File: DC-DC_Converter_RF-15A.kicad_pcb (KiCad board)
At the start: 2 copper layers, 72 x 79 mm, 73 parts, among them K1 G5L-SMALL, Q1 75NF75_TO-220, Q2 75NF75_TO-220, Q3 NPN_SOT23-3_BEC, Q4 NPN_SOT23-3_BEC, Q5 PNP_SOT-223_BCE, Q6 PNP_SOT-223_BCE, U1 TL494

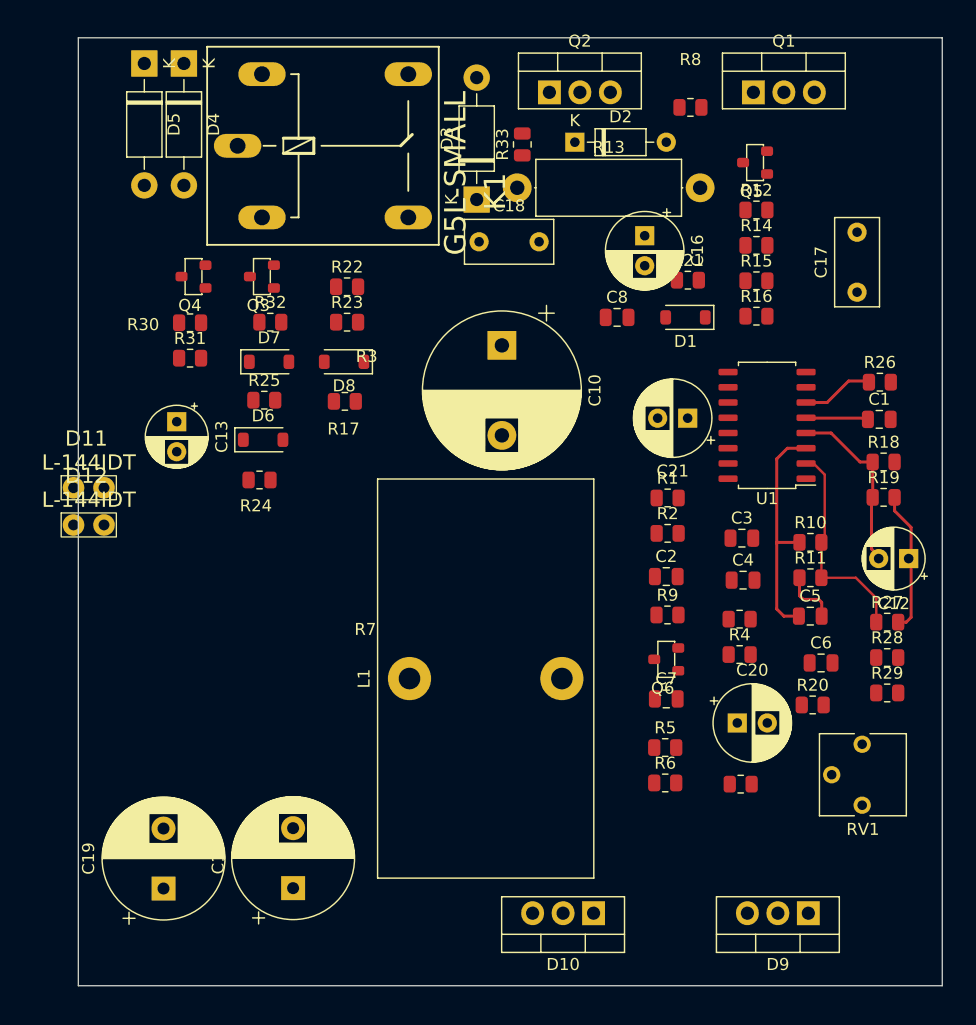
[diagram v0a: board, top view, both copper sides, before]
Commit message: Se termina la PCB, queda acomodar el esquemático
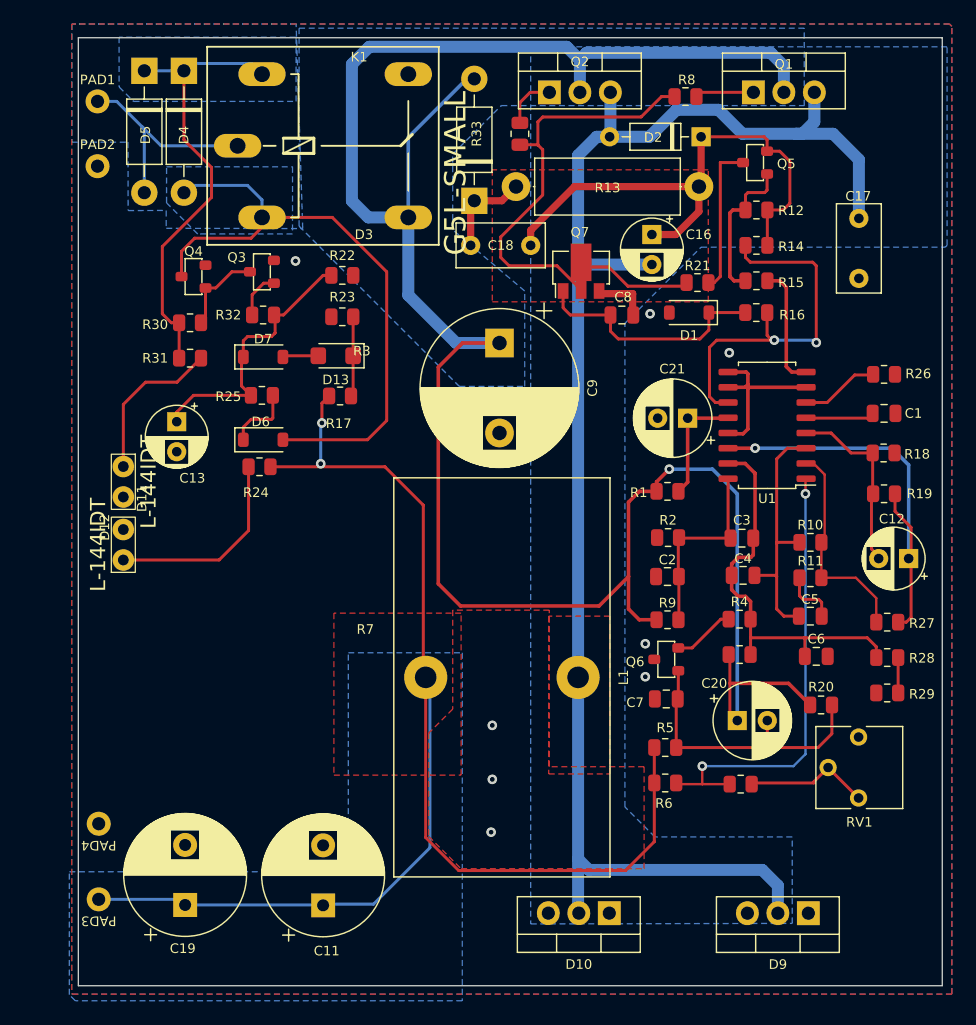
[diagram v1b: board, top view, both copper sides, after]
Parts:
- removed C10: C_Axial, Capacitor_THT:CP_Radial_D13.0mm_P7.50mm
- removed D8: 1N4148W, Diode_SMD:D_SOD-123
- added C9: C_Polarized_US, Capacitor_THT:CP_Radial_D13.0mm_P7.50mm, F.Cu at (131.6, 103.6)
- added D13: BZD27Cxx, Diode_SMD:D_SMF, F.Cu at (118.0, 104.7)
- added PAD1: PAD_2.0_1.1, 1-Pad:PAD_2.0_1.1, F.Cu at (98.1, 83.5)
- added PAD2: PAD_2.0_1.1, 1-Pad:PAD_2.0_1.1, F.Cu at (98.1, 88.9)
- added PAD3: PAD_2.0_1.1, 1-Pad:PAD_2.0_1.1, F.Cu at (98.2, 150.0)
- added PAD4: PAD_2.0_1.1, 1-Pad:PAD_2.0_1.1, F.Cu at (98.2, 143.7)
- added Q7: PXT2222A_SOT-89, 1-Package_TO_SOT_SMD:SOT-89-3, F.Cu at (138.4, 97.7)
- C16: footprint Capacitor_THT:CP_Radial_D6.3mm_P2.50mm -> Capacitor_THT:CP_Radial_D5.0mm_P2.50mm
- moved L1 14.1 mm to (138.2, 131.5), turned to -90 degrees
- moved D2 10.5 mm to (148.4, 86.5), turned to 180 degrees
- moved C17 6.15 mm to (161.6, 93.2), turned to -90 degrees
- moved D12 3.32 mm to (100.2, 120.5), turned to 90 degrees
- moved D11 2.92 mm to (100.2, 115.2), turned to -90 degrees
- moved C11 2.88 mm to (116.9, 150.5)
- moved C19 2.26 mm to (105.4, 150.5)
- moved D10 1.31 mm to (140.8, 151.2)
- moved R24 1.10 mm to (111.6, 114.0)
- moved R22 1.03 mm to (118.5, 98.0)
- moved R8 0.99 mm to (147.1, 83.1)
- moved R33 0.91 mm to (133.3, 86.2)
- moved R32 0.85 mm to (111.9, 101.3)
- moved R21 0.82 mm to (148.1, 98.6)
- moved C18 0.76 mm to (129.2, 95.5)
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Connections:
- C11 pad 1: +BATT -> L1
- C12 pad 1: Net-(C12-Pad1) -> REF
- C13 pad 1: unconnected-(C13-Pad1) -> Net-(D7-K)
- C13 pad 2: unconnected-(C13-Pad2) -> GND
- C16 pad 1: unconnected-(C16-Pad1) -> Net-(D2-K)
- C16 pad 2: unconnected-(C16-Pad2) -> L2
- C17 pad 1: unconnected-(C17-Pad1) -> L2
- C17 pad 2: unconnected-(C17-Pad2) -> GND
- C18 pad 1: unconnected-(C18-Pad1) -> Net-(D3-K)
- C18 pad 2: unconnected-(C18-Pad2) -> Net-(D2-K)
- C19 pad 1: +BATT -> L1
- C2 pad 1: unconnected-(C2-Pad1) -> GND
- C2 pad 2: unconnected-(C2-Pad2) -> IN2+
- C20 pad 1: unconnected-(C20-Pad1) -> +VSW
- C20 pad 2: unconnected-(C20-Pad2) -> Net-(Q6-B)
- C21 pad 1: unconnected-(C21-Pad1) -> VCC
- C21 pad 2: unconnected-(C21-Pad2) -> GND
- C3 pad 1: unconnected-(C3-Pad1) -> IN2+
- C3 pad 2: unconnected-(C3-Pad2) -> IN2-
- C4 pad 1: unconnected-(C4-Pad1) -> IN2-
- C4 pad 2: unconnected-(C4-Pad2) -> FB
- C6 pad 1: unconnected-(C6-Pad1) -> IN2-
- C6 pad 2: unconnected-(C6-Pad2) -> GND
- C7 pad 1: unconnected-(C7-Pad1) -> GND
- C7 pad 2: unconnected-(C7-Pad2) -> Net-(Q6-B)
- C8 pad 1: unconnected-(C8-Pad1) -> Net-(D1-K)
- C8 pad 2: unconnected-(C8-Pad2) -> GND
- D1 pad 1: unconnected-(D1-K-Pad1) -> Net-(D1-K)
- D1 pad 2: unconnected-(D1-A-Pad2) -> GND
- D10 pad 1: unconnected-(D10-A-Pad1) -> GND
- D10 pad 2: unconnected-(D10-K-Pad2) -> L2
- D10 pad 3: unconnected-(D10-A-Pad3) -> GND
- D11 pad A: unconnected-(D11-PadA) -> Net-(D11-PadA)
- D11 pad K: unconnected-(D11-PadK) -> GND
- D2 pad 1: unconnected-(D2-K-Pad1) -> Net-(D2-K)
- D2 pad 2: unconnected-(D2-A-Pad2) -> L2
- D3 pad 1: unconnected-(D3-K-Pad1) -> Net-(D3-K)
- D3 pad 2: unconnected-(D3-A-Pad2) -> +VSW
- D4 pad 1: unconnected-(D4-K-Pad1) -> Net-(D4-K)
- D4 pad 2: unconnected-(D4-A-Pad2) -> Net-(D4-A)
- D5 pad 1: unconnected-(D5-K-Pad1) -> Net-(D4-K)
- D5 pad 2: unconnected-(D5-A-Pad2) -> VBUS
- D6 pad 1: unconnected-(D6-K-Pad1) -> Net-(D6-K)
- D6 pad 2: unconnected-(D6-A-Pad2) -> Net-(D4-A)
- D7 pad 2: Net-(D7-A) -> Net-(D13-A)
- D9 pad 1: unconnected-(D9-A-Pad1) -> GND
- D9 pad 2: unconnected-(D9-K-Pad2) -> L2
- D9 pad 3: unconnected-(D9-A-Pad3) -> GND
- K1 pad 1: unconnected-(K1-Pad1) -> Net-(D4-A)
- K1 pad 2: unconnected-(K1-Pad2) -> Net-(D4-K)
- K1 pad P: unconnected-(K1-PadP) -> VBUS
- K1 pad S: unconnected-(K1-PadS) -> +VSW
- L1 pad 1: unconnected-(L1-Pad1) -> L2
- L1 pad 2: +BATT -> L1
- Q1 pad 1: unconnected-(Q1-G-Pad1) -> Net-(Q1-G)
- Q1 pad 2: unconnected-(Q1-D-Pad2) -> +VSW
- Q1 pad 3: unconnected-(Q1-S-Pad3) -> L2
- Q2 pad 1: unconnected-(Q2-G-Pad1) -> Net-(Q2-G)
- Q2 pad 2: unconnected-(Q2-D-Pad2) -> +VSW
- Q2 pad 3: unconnected-(Q2-S-Pad3) -> L2
- Q3 pad 2: unconnected-(Q3-E-Pad2) -> GND
- Q3 pad 3: unconnected-(Q3-C-Pad3) -> Net-(Q3-C)
- Q4 pad 1: unconnected-(Q4-B-Pad1) -> Net-(Q3-C)
- Q4 pad 2: unconnected-(Q4-E-Pad2) -> GND
- Q4 pad 3: unconnected-(Q4-C-Pad3) -> Net-(D4-A)
- Q5 pad 1: unconnected-(Q5-B-Pad1) -> Net-(Q5-B)
- Q5 pad 2: unconnected-(Q5-E-Pad2) -> Net-(D2-K)
- Q5 pad 3: unconnected-(Q5-C-Pad3) -> Net-(Q5-C)
- Q6 pad 1: unconnected-(Q6-B-Pad1) -> Net-(Q6-B)
- Q6 pad 2: unconnected-(Q6-E-Pad2) -> Net-(Q6-E)
- Q6 pad 3: unconnected-(Q6-C-Pad3) -> GND
- R1 pad 1: unconnected-(R1-Pad1) -> +VSW
- R1 pad 2: unconnected-(R1-Pad2) -> VCC
- R12 pad 1: unconnected-(R12-Pad1) -> Net-(Q5-B)
- R12 pad 2: unconnected-(R12-Pad2) -> Net-(D2-K)
- R13 pad 1: unconnected-(R13-Pad1) -> Net-(D3-K)
- R13 pad 2: unconnected-(R13-Pad2) -> Net-(D2-K)
- R14 pad 1: unconnected-(R14-Pad1) -> C2
- R14 pad 2: unconnected-(R14-Pad2) -> Net-(D2-K)
- R15 pad 1: unconnected-(R15-Pad1) -> Net-(Q5-B)
- R15 pad 2: unconnected-(R15-Pad2) -> C1
- R16 pad 1: unconnected-(R16-Pad1) -> Net-(D1-K)
- R16 pad 2: unconnected-(R16-Pad2) -> C2
- R17 pad 1: +BATT -> L1
- R17 pad 2: Net-(D8-K) -> Net-(D13-K)
- R19 pad 2: Net-(C12-Pad1) -> REF
- R2 pad 1: unconnected-(R2-Pad1) -> GND
- R2 pad 2: unconnected-(R2-Pad2) -> IN2+
- R20 pad 1: unconnected-(R20-Pad1) -> +VSW
- R20 pad 2: unconnected-(R20-Pad2) -> Net-(Q6-B)
- R21 pad 1: unconnected-(R21-Pad1) -> Net-(Q7-C)
- R21 pad 2: unconnected-(R21-Pad2) -> Net-(Q5-C)
- R22 pad 1: unconnected-(R22-Pad1) -> Net-(D7-K)
- R22 pad 2: unconnected-(R22-Pad2) -> GND
- R23 pad 2: Net-(D7-A) -> Net-(D13-K)
- R24 pad 2: +BATT -> L1
- R25 pad 2: unconnected-(R25-Pad2) -> Net-(D6-K)
- R27 pad 2: Net-(C12-Pad1) -> REF
- R28 pad 1: unconnected-(R28-Pad1) -> IN2-
- R28 pad 2: unconnected-(R28-Pad2) -> Net-(R28-Pad2)
- R29 pad 1: unconnected-(R29-Pad1) -> Net-(R28-Pad2)
- R29 pad 2: unconnected-(R29-Pad2) -> GND
- R3 pad 1: unconnected-(R3-Pad1) -> Net-(Q6-E)
- R3 pad 2: unconnected-(R3-Pad2) -> IN2-
- R30 pad 1: unconnected-(R30-Pad1) -> Net-(D4-K)
- R30 pad 2: unconnected-(R30-Pad2) -> Net-(Q3-C)
- R31 pad 1: unconnected-(R31-Pad1) -> Net-(D4-K)
- R31 pad 2: unconnected-(R31-Pad2) -> Net-(D11-PadA)
- R32 pad 1: Net-(D7-K) -> Net-(Q3-B)
- R32 pad 2: Net-(Q3-B) -> Net-(D7-K)
- R33 pad 1: unconnected-(R33-Pad1) -> Net-(Q7-C)
- R33 pad 2: unconnected-(R33-Pad2) -> Net-(Q2-G)
- R4 pad 1: unconnected-(R4-Pad1) -> +VSW
- R4 pad 2: unconnected-(R4-Pad2) -> IN2-
- R5 pad 1: unconnected-(R5-Pad1) -> L1
- R5 pad 2: unconnected-(R5-Pad2) -> Net-(Q6-B)
- R6 pad 1: +BATT -> L1
- R6 pad 2: IN1- -> IN1+
- R7 pad 1: IN1- -> IN1+
- R8 pad 1: unconnected-(R8-Pad1) -> Net-(Q7-C)
- R8 pad 2: unconnected-(R8-Pad2) -> Net-(Q1-G)
- R9 pad 1: unconnected-(R9-Pad1) -> +VSW
- R9 pad 2: unconnected-(R9-Pad2) -> IN2+
- RV1 pad 1: Net-(R7-Pad2) -> GND
- RV1 pad 3: GND -> Net-(R7-Pad2)
- U1 pad 10: unconnected-(U1-E2-Pad10) -> GND
- U1 pad 11: unconnected-(U1-C2-Pad11) -> C2
- U1 pad 12: unconnected-(U1-VCC-Pad12) -> VCC
- U1 pad 13: unconnected-(U1-OUTCTRL-Pad13) -> GND
- U1 pad 14: unconnected-(U1-REF-Pad14) -> REF
- U1 pad 7: unconnected-(U1-GND-Pad7) -> GND
- U1 pad 8: unconnected-(U1-C1-Pad8) -> C1
- U1 pad 9: unconnected-(U1-E1-Pad9) -> GND
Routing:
- net +VSW: track 0.00 -> 186.1 mm, vias 0 -> 1
- net L2: track 0.00 -> 128.9 mm
- net L1: track 0.00 -> 121.0 mm, vias 0 -> 2
- net Net-(D4-A): track 0.00 -> 53.2 mm
- net Net-(Q7-C): track 0.00 -> 46.0 mm
- net Net-(D2-K): track 0.00 -> 45.2 mm
- net IN1+: track 0.00 -> 38.0 mm, vias 0 -> 2
- net Net-(D4-K): track 0.00 -> 38.0 mm
- net REF: track 0.00 -> 35.5 mm, vias 0 -> 1
- net IN2-: track 0.00 -> 33.4 mm
- net C2: track 0.00 -> 31.5 mm, vias 0 -> 2
- net Net-(Q6-B): track 0.00 -> 24.6 mm
- net Net-(D7-K): track 0.00 -> 23.1 mm
- net Net-(D1-K): track 0.00 -> 20.3 mm
- net GND: track 0.00 -> 19.5 mm, vias 0 -> 8
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- added copper zone on B.Cu, net +VSW
- added copper zone on B.Cu, net GND
- added copper zone on F.Cu, net GND
- added copper zone on B.Cu, net L1
- added copper zone on F.Cu, net L1
- added copper zone on B.Cu, net L2
- added copper zone on F.Cu, net L2
- added copper zone on B.Cu, net Net-(D4-A)
- added copper zone on B.Cu, net Net-(D4-K)
- added copper zone on F.Cu, net Net-(Q7-C)
- added copper zone on B.Cu, net VBUS

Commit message: Se añadieron los valores de algunos componentes, falta ordenar
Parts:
- removed R13: R_Axial_DIN0414_L11.9mm_D4.5mm_P15.24mm_Horizontal_1W, 1-Resistor:R_Axial_DIN0414_L11.9mm_D4.5mm_P15.24mm_Horizontal_1W
- removed U1: TL494, 1-Package_SO:SOIC-16_4.55x10.3mm_P1.27mm
- added 470R1: R_Axial_DIN0414_L11.9mm_D4.5mm_P15.24mm_Horizontal_1W, 1-Resistor:R_Axial_DIN0414_L11.9mm_D4.5mm_P15.24mm_Horizontal_1W, F.Cu at (133.1, 90.6)
- added U2: TL494_SOIC-16, 1-Package_SO:SOIC-16_4.55x10.3mm_P1.27mm, F.Cu at (153.9, 110.5)
- C11, C19: value C_Polarized_US -> 2200uF 16V
- C17: value rect -> 1nF 100V
- C18: value rect -> 100nF
- R1, R7: value R_0805 -> 560R
- R10: value R_0805 -> 1M
- R11: value R_0805 -> 47k
- R12, R14, R16, R18, R20, R22, R23, R30, R32, R6: value R_0805 -> 10k
- R15, R3: value R_0805 -> 5.1k
- R17: value R_0805 -> 6.2k
- R19: value R_0805 -> 75k
- R2, R28, R4, R9: value R_0805 -> 100k
- R21, R33, R8: value R_0805 -> 100R
- R24, R29, R5: value R_0805 -> 3.3k
- R25: value R_0805 -> 22k
- R26: value R_0805 -> 39k
- R27, R31: value R_0805 -> 4.7k
- moved R5 0.66 mm to (145.5, 136.7)
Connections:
- net IN1+ renamed Net-(U2-1IN+)
- net REF renamed +5V
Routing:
- net L1: track 121.0 -> 121.6 mm
- net Net-(D11-PadA): track 13.2 -> 13.8 mm
